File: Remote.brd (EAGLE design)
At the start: 100 x 27.9 mm, 15 parts

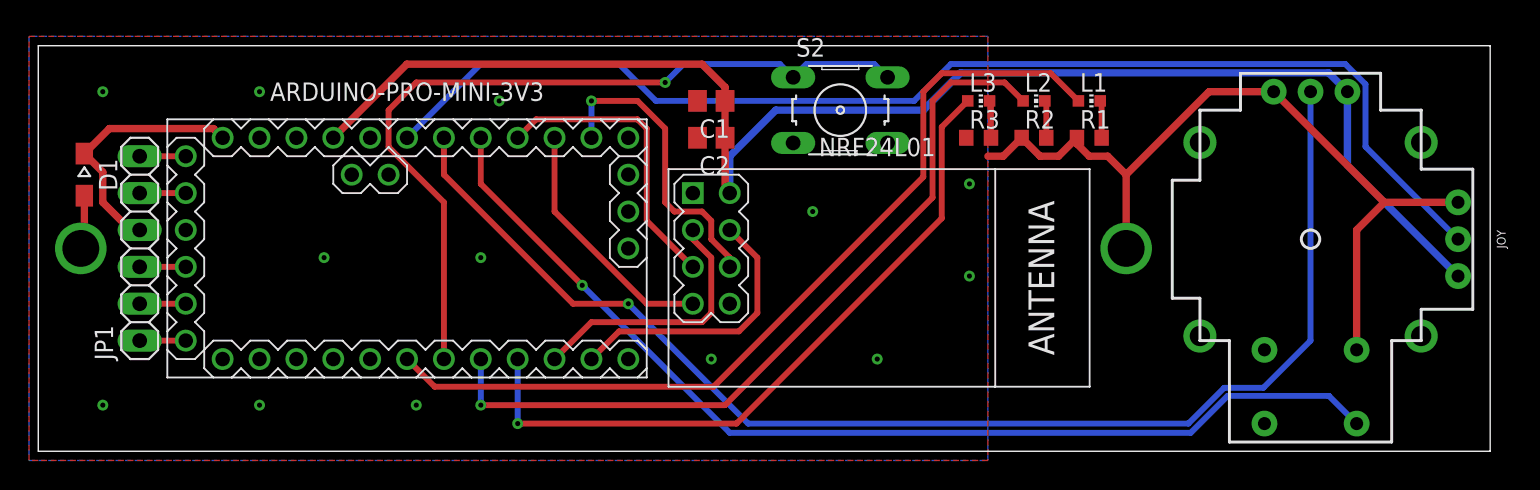
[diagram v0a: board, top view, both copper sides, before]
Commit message: GND trace width change. Updated silkscreen and created CAM files
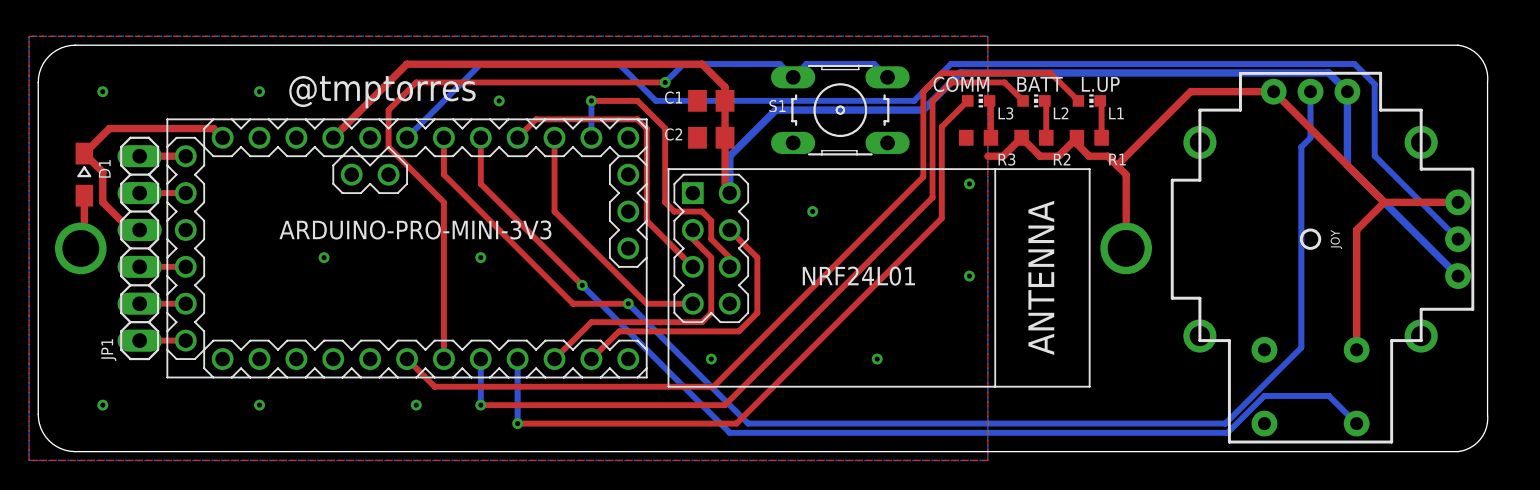
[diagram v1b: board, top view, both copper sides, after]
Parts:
- U$2: device battery-holders:BLOSSOM-BLM-18650-1PCS-NO-SCREWS-SMALL-HOLES -> battery-holders-modified:BLOSSOM-BLM-18650-1PCS-NO-SCREWS-SMALL-HOLES
- renumbered S2 to S1
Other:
- board size 100 x 27.9 mm -> 99.8 x 28 mm
- board text added: "@tmptorres"
- board text added: "BATT"
- board text added: "COMM"
- board text added: "JLCJLCJLCJLC"
- board text added: "L.UP"
